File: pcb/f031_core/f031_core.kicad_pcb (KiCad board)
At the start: 2 copper layers, 99.1 x 99.1 mm, 34 parts, among them J1 Conn_02x13_Odd_Even, J2 Conn_02x13_Odd_Even, SW1 SW_Push, U1 STM32F031C6Tx, U2 AMS1117-3.3, Y1 8M, Y2 32768HZ

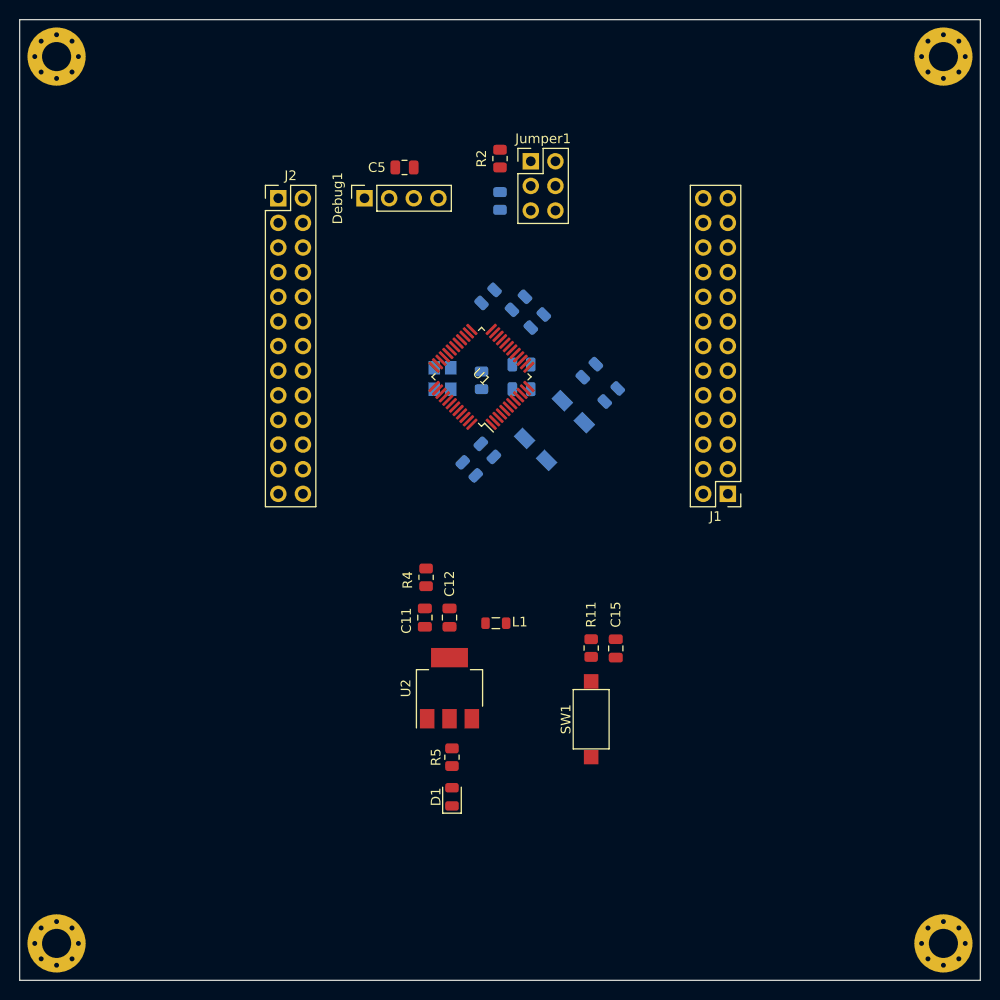
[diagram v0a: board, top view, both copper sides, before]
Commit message: Put more components to back.
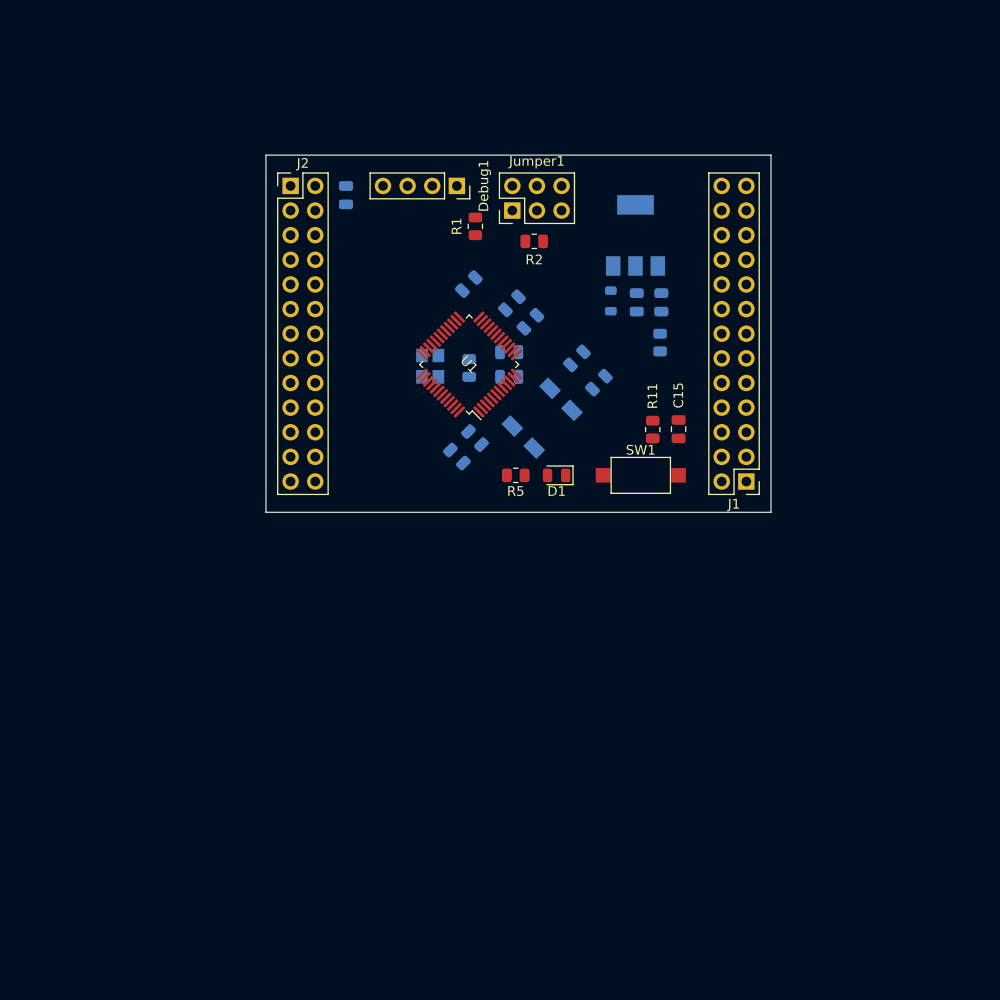
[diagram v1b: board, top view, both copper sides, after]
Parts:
- removed Pad1, Pad2, Pad3, Pad4: MountingHole_3mm_Pad_Via, MountingHole:MountingHole_3mm_Pad_Via
- C11, C12, C5, L1, R4, U2: moved to B.Cu
- R1: moved to F.Cu
- moved U2 50.5 mm to (101.6, 47.6)
- moved C11 40.6 mm to (104.3, 54.5), turned to 270 degrees
- moved C12 37.8 mm to (101.7, 54.5), turned to 270 degrees
- moved L1 35.3 mm to (99.1, 54.4), turned to 270 degrees
- moved D1 34.9 mm to (93.5, 72.4), turned to 180 degrees
- moved R4 34.2 mm to (104.1, 58.7), turned to 270 degrees
- moved R5 29.8 mm to (89.3, 72.4), turned to 180 degrees
- moved SW1 25.7 mm to (102.1, 72.4), turned to 0 degrees
- moved C15 23.5 mm to (106.0, 67.6)
- moved R11 23.4 mm to (103.4, 67.7)
- moved Debug1 9.61 mm to (83.2, 42.5), turned to 270 degrees
- moved R2 9.23 mm to (91.2, 48.3), turned to 0 degrees
- moved C5 6.67 mm to (71.8, 43.5), turned to 270 degrees
- moved Jumper1 5.43 mm to (88.9, 45.1), turned to 90 degrees
- moved R1 3.65 mm to (85.1, 46.7)
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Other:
- board size 99.1 x 99.1 mm -> 52.1 x 36.8 mm

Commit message: Complete f031_core board.
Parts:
- removed Debug1: Conn_01x04, Connector_PinSocket_2.54mm:PinSocket_1x04_P2.54mm_Vertical
- removed Jumper1: Conn_02x03_Odd_Even, Connector_PinHeader_2.54mm:PinHeader_2x03_P2.54mm_Vertical
- added J3: USB_B_Mini, Connector_USB:USB_Mini-B_AdamTech_MUSB-B5-S-VT-TSMT-1_SMD_Vertical, B.Cu at (92.2, 42.9)
- added J4: Conn_01x04, Connector_PinSocket_2.54mm:PinSocket_1x04_P2.54mm_Vertical, F.Cu at (71.8, 41.3)
- added J5: Conn_02x03_Odd_Even, Connector_PinHeader_2.54mm:PinHeader_2x03_P2.54mm_Vertical, F.Cu at (77.5, 43.8)
- moved J2 12.8 mm to (53.3, 41.3)
- moved R1 11.5 mm to (73.7, 45.4)
- moved C5 11.5 mm to (60.3, 42.2)
- moved R2 11.5 mm to (79.7, 47.0)
- moved C6 8.98 mm to (75.5, 51.4)
- moved C9 8.98 mm to (81.9, 55.3)
- moved C10 8.98 mm to (80.0, 53.4)
- moved C3 8.98 mm to (88.9, 61.6)
- moved J1 8.98 mm to (104.1, 71.8)
- moved R11 8.98 mm to (94.5, 66.4)
- moved R3 8.98 mm to (75.6, 60.0)
- moved U1 8.98 mm to (75.6, 59.7)
- moved Y1 8.98 mm to (71.5, 59.9)
- moved C1 8.98 mm to (79.7, 61.0)
- moved C15 8.98 mm to (97.2, 66.4)
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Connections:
- J1 pad 1: Net-(J1-Pad1) -> GNDA
- J1 pad 2: Net-(J1-Pad2) -> +3.3VA
- J1 pad 3: Net-(J1-Pad3) -> GNDA
- J1 pad 4: Net-(J1-Pad4) -> +3.3VA
- J1 pad 5: +3V3 -> GND
- J1 pad 6: +3.3VA -> +3V3
- J1 pad 8: GNDA -> +3V3
- J2 pad 23: +3V3 -> GND
- J2 pad 25: +3V3 -> GND
- J2 pad 26: GND -> +3V3
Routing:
- net GND: track 0.00 -> 235.4 mm
- net +3V3: track 0.00 -> 216.2 mm
- net /PB10: track 0.00 -> 55.8 mm, vias 0 -> 1
- net /PA13: track 0.00 -> 43.3 mm
- net RESET: track 0.00 -> 42.0 mm
- net +3.3VA: track 0.00 -> 41.1 mm, vias 0 -> 1
- net /PB14: track 0.00 -> 37.2 mm
- net /PB11: track 0.00 -> 35.6 mm
- net GNDA: track 0.00 -> 31.0 mm, vias 0 -> 1
- net /PB0: track 0.00 -> 29.8 mm
- net /PA7: track 0.00 -> 28.5 mm
- net /PB1: track 0.00 -> 28.0 mm, vias 0 -> 1
- net /PA5: track 0.00 -> 27.0 mm
- net /PC13: track 0.00 -> 27.0 mm
- net /PB13: track 0.00 -> 26.1 mm
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- added copper zone on B.Cu, net GND
- added copper zone on F.Cu, net GND
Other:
- board size 52.1 x 36.8 mm -> 55.9 x 36.8 mm

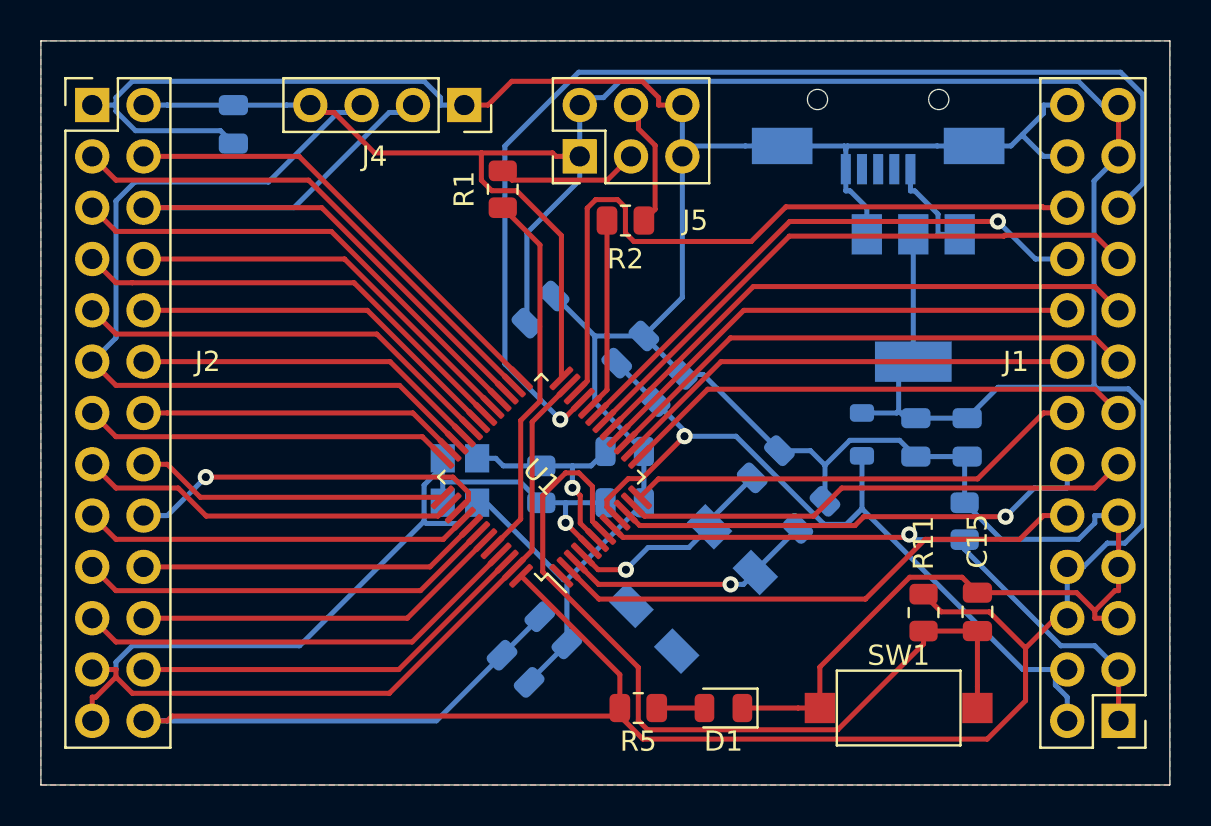
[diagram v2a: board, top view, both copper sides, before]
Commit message: Fix layout of f031_core board.
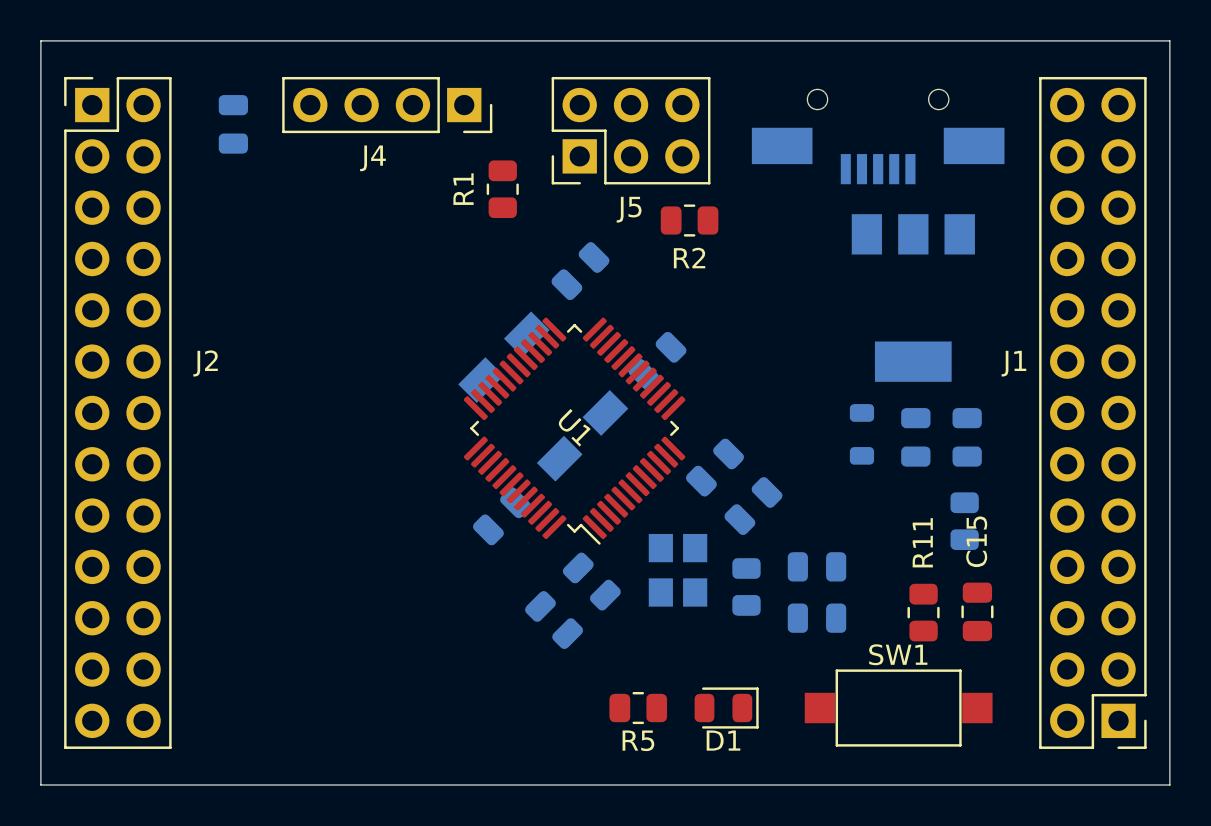
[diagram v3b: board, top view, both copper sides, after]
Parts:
- moved C3 15.3 mm to (73.6, 61.6), turned to 45 degrees
- moved Y2 12.1 mm to (75.7, 55.7), turned to 45 degrees
- moved Y1 11.7 mm to (82.3, 64.3)
- moved R3 11.4 mm to (85.7, 65.1)
- moved C2 11.1 mm to (89.2, 64.1)
- moved C1 11.1 mm to (89.2, 66.7)
- moved C4 7.41 mm to (81.3, 53.9)
- moved C9 7.19 mm to (86.1, 61.1)
- moved C10 7.19 mm to (84.2, 59.2)
- moved R2 3.17 mm to (82.9, 47.0)
- moved C7 3.07 mm to (76.2, 66.8)
- moved C8 3.07 mm to (78.1, 64.9)
- moved U1 2.92 mm to (77.2, 57.3)
- moved C6 2.75 mm to (77.5, 49.5)
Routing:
- net GND: track 235.4 -> 0.00 mm
- net +3V3: track 216.2 -> 0.00 mm
- net /PB10: track 55.8 -> 0.00 mm, vias 1 -> 0
- net /PA13: track 43.3 -> 0.00 mm
- net RESET: track 42.0 -> 0.00 mm
- net +3.3VA: track 41.1 -> 0.00 mm, vias 1 -> 0
- net /PB14: track 37.2 -> 0.00 mm
- net /PB11: track 35.6 -> 0.00 mm
- net GNDA: track 31.0 -> 0.00 mm, vias 1 -> 0
- net /PB0: track 29.8 -> 0.00 mm
- net /PA7: track 28.5 -> 0.00 mm
- net /PB1: track 28.0 -> 0.00 mm, vias 1 -> 0
- net /PA5: track 27.0 -> 0.00 mm
- net /PC13: track 27.0 -> 0.00 mm
- net /PB13: track 26.1 -> 0.00 mm
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- removed copper zone on B.Cu, net GND
- removed copper zone on F.Cu, net GND

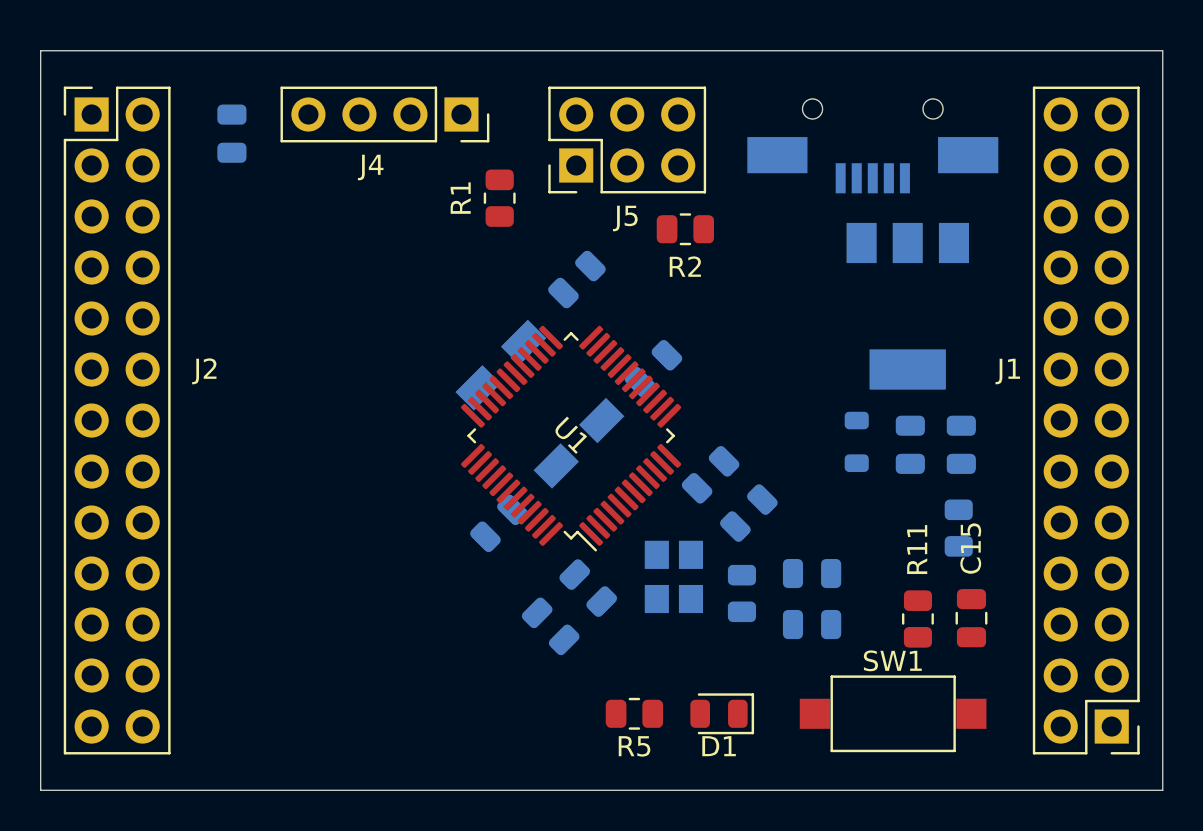
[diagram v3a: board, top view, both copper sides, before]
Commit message: Update layout of f031 & f103 boards.
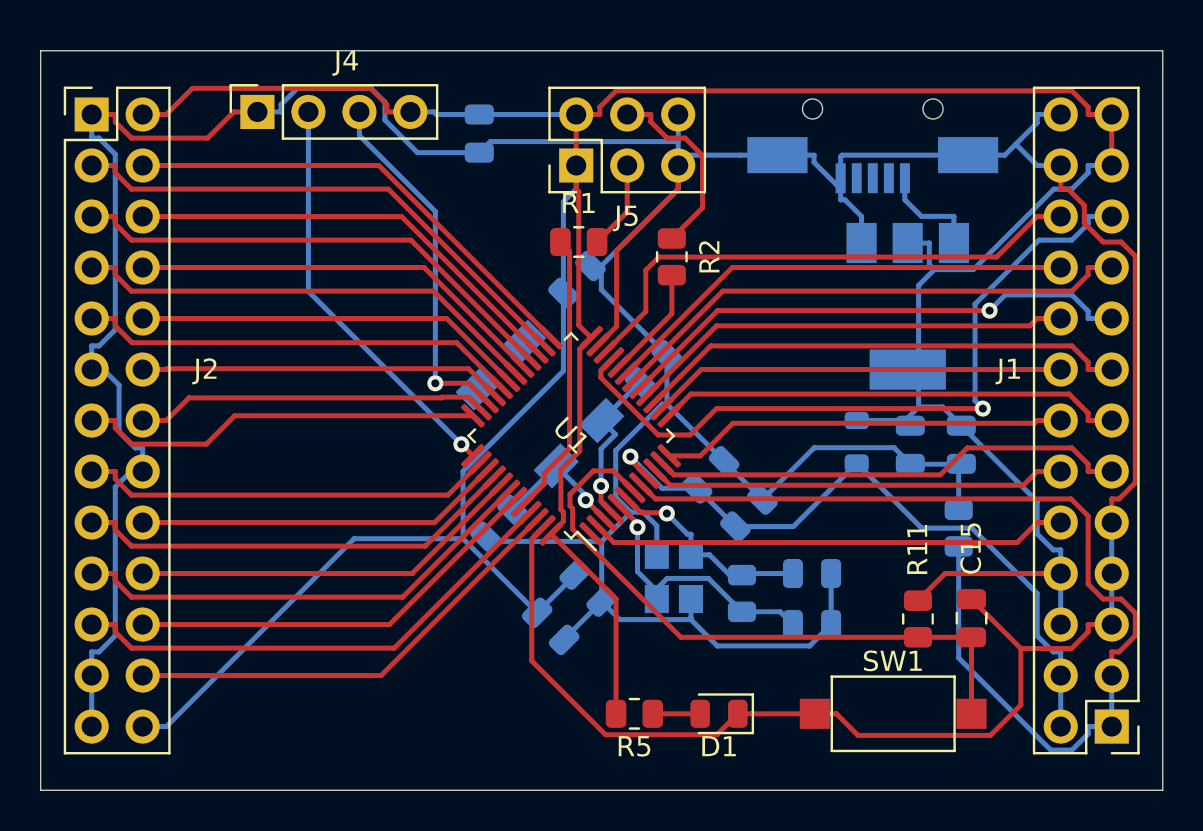
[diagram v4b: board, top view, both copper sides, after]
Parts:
- moved C5 12.3 mm to (72.6, 42.2)
- moved J4 10.2 mm to (61.6, 41.1), turned to 90 degrees
- moved R1 4.50 mm to (77.6, 47.6), turned to 180 degrees
- moved R2 1.53 mm to (82.2, 48.4), turned to 90 degrees
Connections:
- J2 pad 11: /PA13 -> GND
- J2 pad 16: /PA14 -> GND
- J4 pad 2: /PB14 -> /SYS_SWCL
- J4 pad 3: /PA13 -> /SYS_SWDIO
- U1 pad 34: /PA13 -> /SYS_SWDIO
- U1 pad 37: /PA14 -> /SYS_SWCL
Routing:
- net GND: track 0.00 -> 257.8 mm
- net +3V3: track 0.00 -> 182.1 mm
- net GNDA: track 0.00 -> 51.4 mm
- net /PB10: track 0.00 -> 36.1 mm, vias 0 -> 1
- net +3.3VA: track 0.00 -> 34.4 mm, vias 0 -> 1
- net RESET: track 0.00 -> 31.8 mm
- net /PB11: track 0.00 -> 26.7 mm
- net /PB13: track 0.00 -> 26.4 mm
- net /PB0: track 0.00 -> 26.3 mm
- net /PA7: track 0.00 -> 26.1 mm, vias 0 -> 1
- net /PB8: track 0.00 -> 25.3 mm
- net /PB15: track 0.00 -> 25.0 mm
- net /PA5: track 0.00 -> 24.6 mm
- net /PA1: track 0.00 -> 23.9 mm
- net /PB12: track 0.00 -> 23.9 mm
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
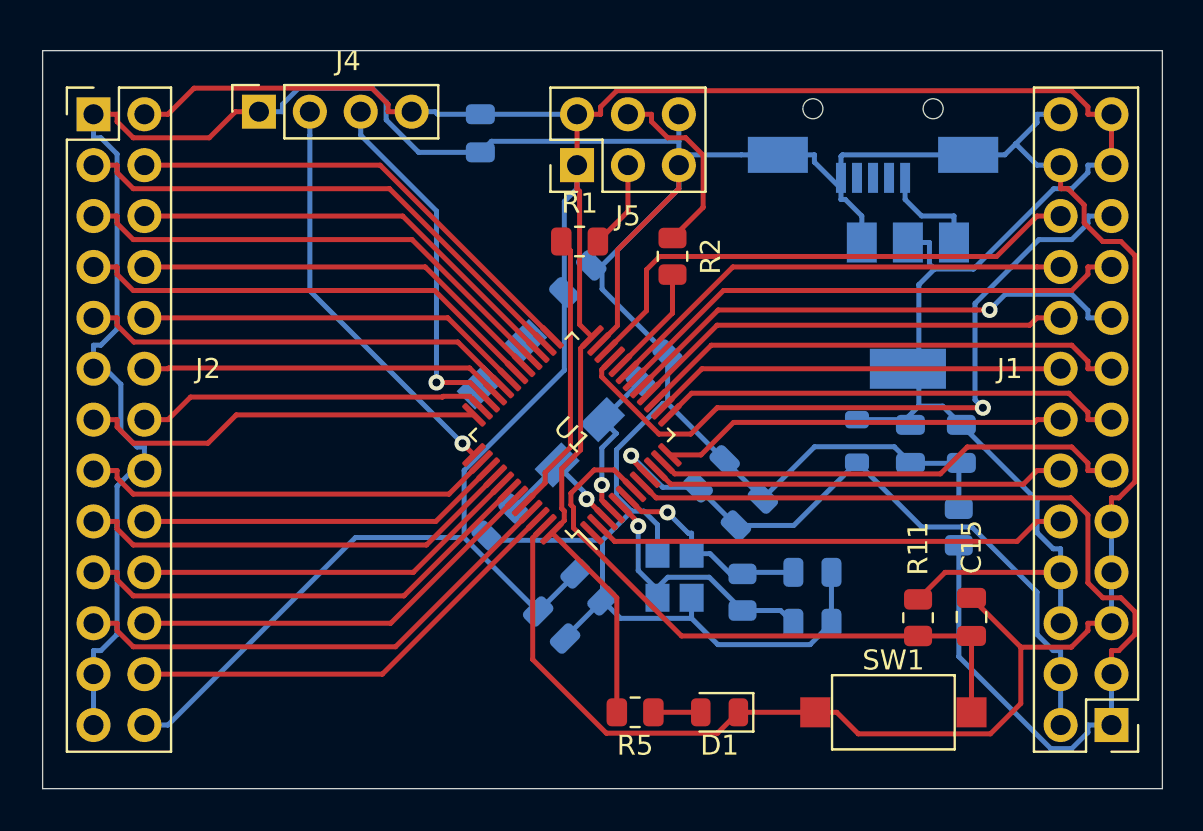
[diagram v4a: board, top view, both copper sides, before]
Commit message: Add routing keypoints for capacitors.
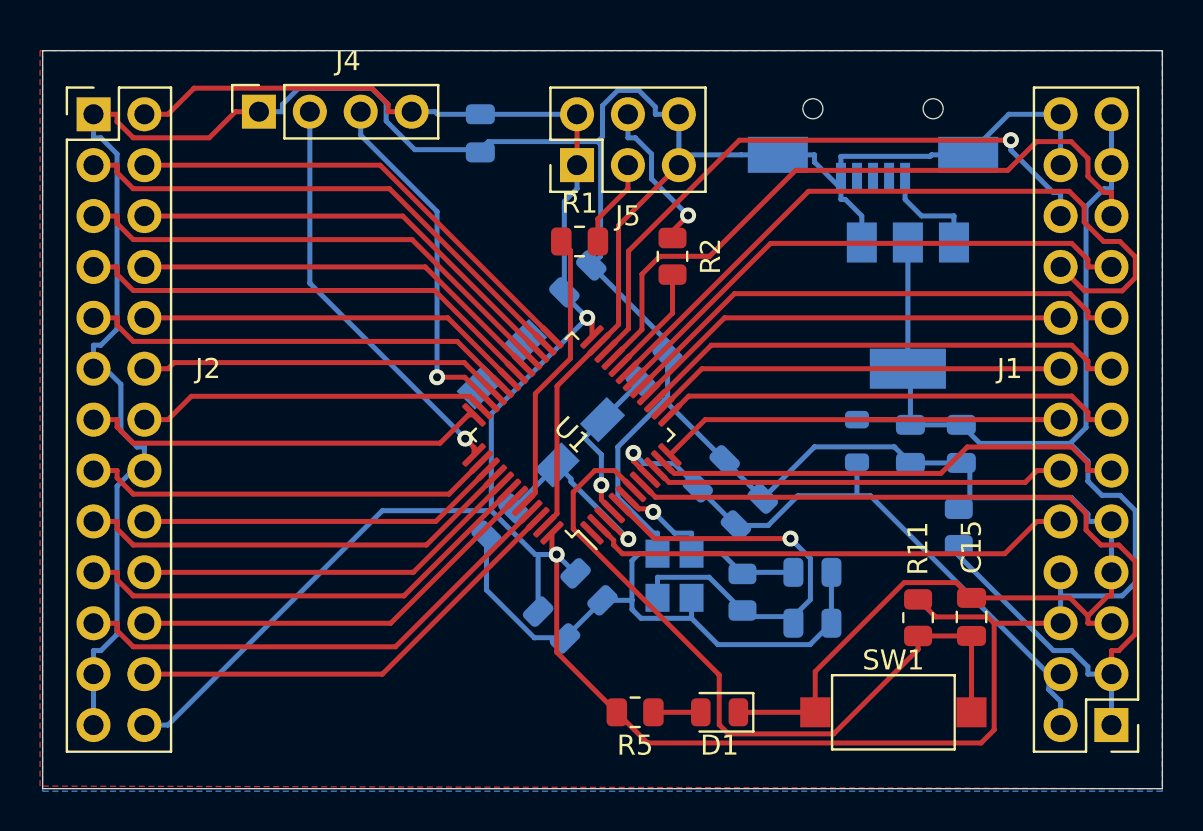
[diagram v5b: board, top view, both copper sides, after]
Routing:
- net GND: track 257.8 -> 235.3 mm
- net /PB1: track 23.8 -> 36.4 mm
- net /RCC_OSC_IN: track 13.4 -> 22.8 mm
- net +3V3: track 182.1 -> 173.0 mm, vias 0 -> 2
- net RESET: track 31.8 -> 37.5 mm
- net /PB11: track 26.7 -> 31.9 mm, vias 0 -> 1
- net GNDA: track 51.4 -> 46.4 mm
- net /RCC_OSC32_IN: track 6.78 -> 9.78 mm
- net /PB10: track 36.1 -> 33.7 mm, vias 1 -> 0
- net Net-(J5-Pad4): track 9.58 -> 7.96 mm, vias 0 -> 1
- net +3.3VA: track 34.4 -> 33.0 mm
- net /PB0: track 26.3 -> 27.3 mm
- net /PC13: track 23.8 -> 24.4 mm
- net /PA7: vias 1 -> 0
- added copper zone on B.Cu, net GND
- added copper zone on F.Cu, net GND
